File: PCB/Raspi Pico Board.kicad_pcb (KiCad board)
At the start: 4 copper layers, 66 x 32.3 mm, 78 parts, among them J1 USB4105, J2 Conn_01x03_Pin, J3 Conn_01x12_Pin, J4 Conn_01x03_Pin, J5 Conn_01x03_Pin, SW1 SW_Push, SW2 SW_Push, SW3 SW_Push, U1 RP2040, U2 W25Q128JV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

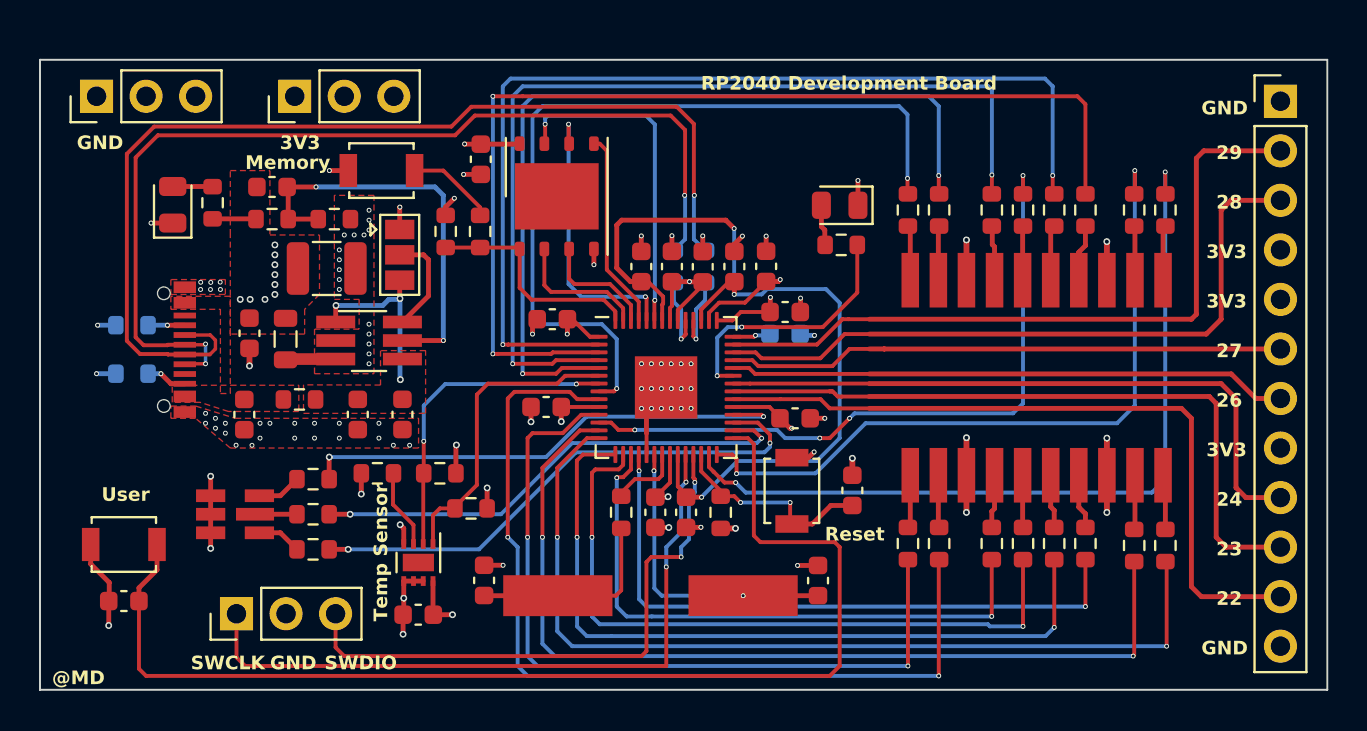
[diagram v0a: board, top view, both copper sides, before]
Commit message: Layout changed, USB-C socket moved on the other side of the PCB, almost complted. DRC to be done
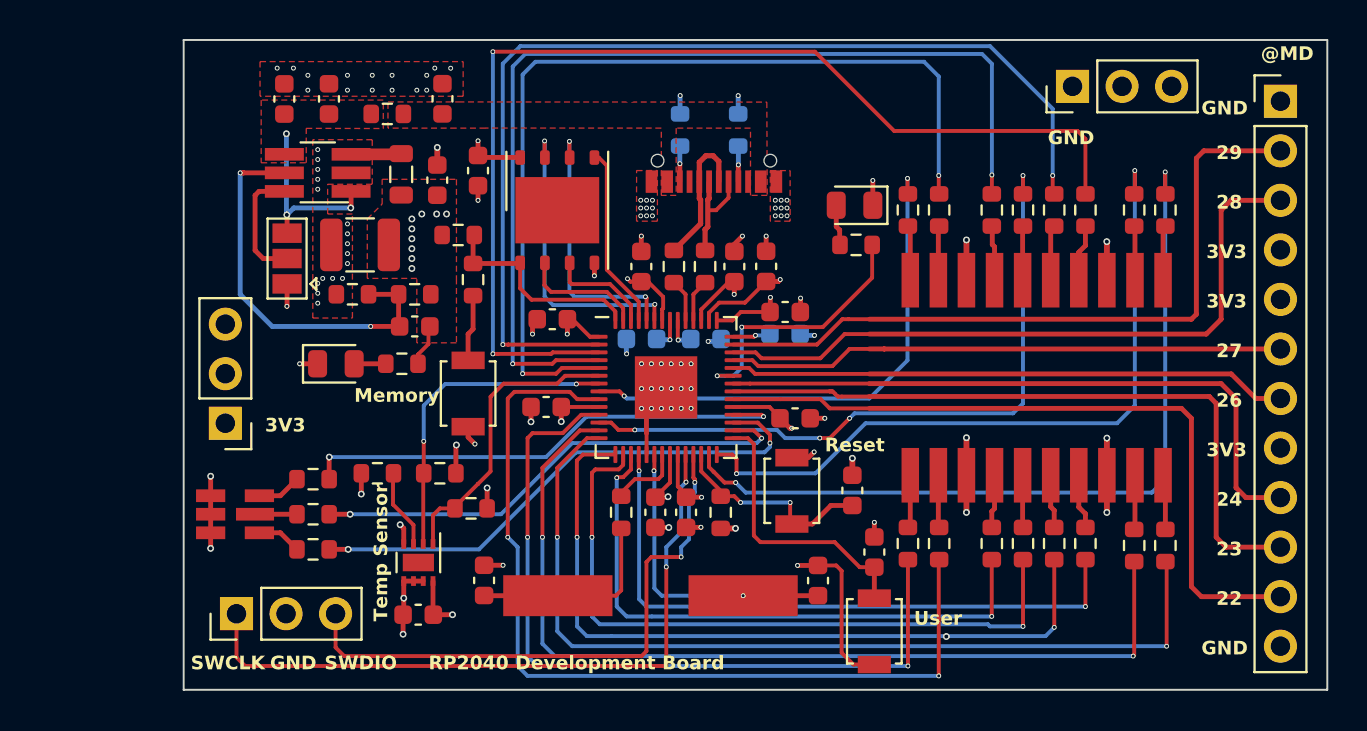
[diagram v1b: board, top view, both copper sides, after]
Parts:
- C18, C7: moved to B.Cu
- R10, R9: moved to F.Cu
- moved J4 50.0 mm to (100.8, 38.9)
- moved SW3 38.7 mm to (90.7, 66.8), turned to -90 degrees
- moved C23 38.6 mm to (90.7, 62.7), turned to -90 degrees
- moved R1 32.7 mm to (83.7, 41.1), turned to -90 degrees
- moved R2 30.8 mm to (80.7, 41.1), turned to -90 degrees
- moved J1 29.2 mm to (82.5, 43.2), turned to 180 degrees
- moved C1 19.1 mm to (68.5, 39.5), turned to 90 degrees
- moved C3 17.3 mm to (60.4, 39.5), turned to 90 degrees
- moved J5 17.1 mm to (57.4, 56.1), turned to 180 degrees
- moved C2 16.2 mm to (62.7, 39.5), turned to 90 degrees
- moved FB1 15.3 mm to (65.7, 40.3), turned to 180 degrees
- moved R5 12.7 mm to (66.5, 53.1), turned to 180 degrees
- moved C5 12.4 mm to (68.3, 43.7), turned to 90 degrees
- moved SW2 12.3 mm to (69.8, 54.6), turned to 90 degrees
- moved D1 11.7 mm to (63.1, 53.1), turned to 0 degrees
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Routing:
- net /Microcontroller/USB_N: track 53.9 -> 5.70 mm, vias 1 -> 0
- net /Microcontroller/USER_BUTTON: track 59.7 -> 14.3 mm
- net /Microcontroller/USB_P: track 50.9 -> 7.41 mm, vias 3 -> 0
- net /Microcontroller/display_E1: track 42.2 -> 26.9 mm
- net +1V1: track 43.8 -> 29.7 mm
- net +3V3: track 41.5 -> 37.9 mm
- net /Microcontroller/display_D1: track 44.0 -> 47.3 mm
- net /Microcontroller/display_C1: track 48.4 -> 51.5 mm
- net GND: track 51.4 -> 54.5 mm, vias 98 -> 104
- net /Microcontroller/display_D2: track 53.8 -> 56.0 mm
- net /Microcontroller/USB_M_P: track 4.38 -> 2.19 mm, vias 1 -> 0
- net /Microcontroller/USB_M_N: track 4.09 -> 2.19 mm, vias 1 -> 0
- net /Microcontroller/QSPI_SD3: track 17.2 -> 15.5 mm
- net /Microcontroller/display_E2: track 52.2 -> 53.6 mm
- net Net-(R7-Pad1): track 4.55 -> 3.53 mm
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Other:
- board size 66 x 32.3 mm -> 58.6 x 33.3 mm

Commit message: Layout finished, gerber files generated, ready to send the design to manufacturer
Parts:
- moved J4 0.42 mm to (100.6, 38.5)
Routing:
- net /Microcontroller/display_E1: track 26.9 -> 27.7 mm
- net GND: track 54.5 -> 54.2 mm, vias 104 -> 118
- net /Microcontroller/display_G2: track 38.9 -> 39.2 mm, vias 3 -> 2
- net +3V3: vias 24 -> 37
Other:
- board text removed: "@MD"
- board text removed: "SWCLK"
- board text removed: "SWDIO"
- board text removed: "Temp Sensor"
